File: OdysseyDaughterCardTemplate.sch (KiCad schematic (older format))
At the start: 1 part, among them X1 OdysseyDaughterCard

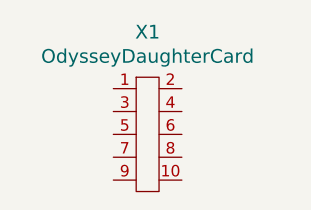
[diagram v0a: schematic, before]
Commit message: Add labels to connector
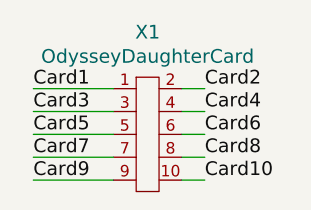
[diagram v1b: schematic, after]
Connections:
- net Card1: now reaches X1.1
- net Card10: now reaches X1.10
- net Card2: now reaches X1.2
- net Card3: now reaches X1.3
- net Card4: now reaches X1.4
- net Card5: now reaches X1.5
- net Card6: now reaches X1.6
- net Card7: now reaches X1.7
- net Card8: now reaches X1.8
- net Card9: now reaches X1.9
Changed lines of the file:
@@
 	1    0    0    -1
 $EndComp
+Wire Wire Line
+	5850 3500 5950 3500
+Wire Wire Line
+	5850 3600 5950 3600
+Wire Wire Line
+	5850 3700 5950 3700
+Wire Wire Line
+	5850 3800 5950 3800
+Wire Wire Line
+	5850 3900 5950 3900
+Text Label 5950 3500 0    60   ~ 0
+Card2
+Text Label 5950 3600 0    60   ~ 0
+Card4
+Text Label 5950 3700 0    60   ~ 0
+Card6
+Text Label 5950 3800 0    60   ~ 0
+Card8
+Text Label 5950 3900 0    60   ~ 0
+Card10
+Wire Wire Line
+	5200 3500 5550 3500
+Text Label 5200 3500 0    60   ~ 0
+Card1
+Text Label 5200 3600 0    60   ~ 0
+Card3
+Text Label 5200 3700 0    60   ~ 0
+Card5
+Text Label 5200 3800 0    60   ~ 0
+Card7
+Text Label 5200 3900 0    60   ~ 0
+Card9
+Wire Wire Line
+	5550 3600 5200 3600
+Wire Wire Line
+	5550 3700 5200 3700
+Wire Wire Line
+	5550 3800 5200 3800
+Wire Wire Line
+	5550 3900 5200 3900
 $EndSCHEMATC
